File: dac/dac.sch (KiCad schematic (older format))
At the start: 0 parts

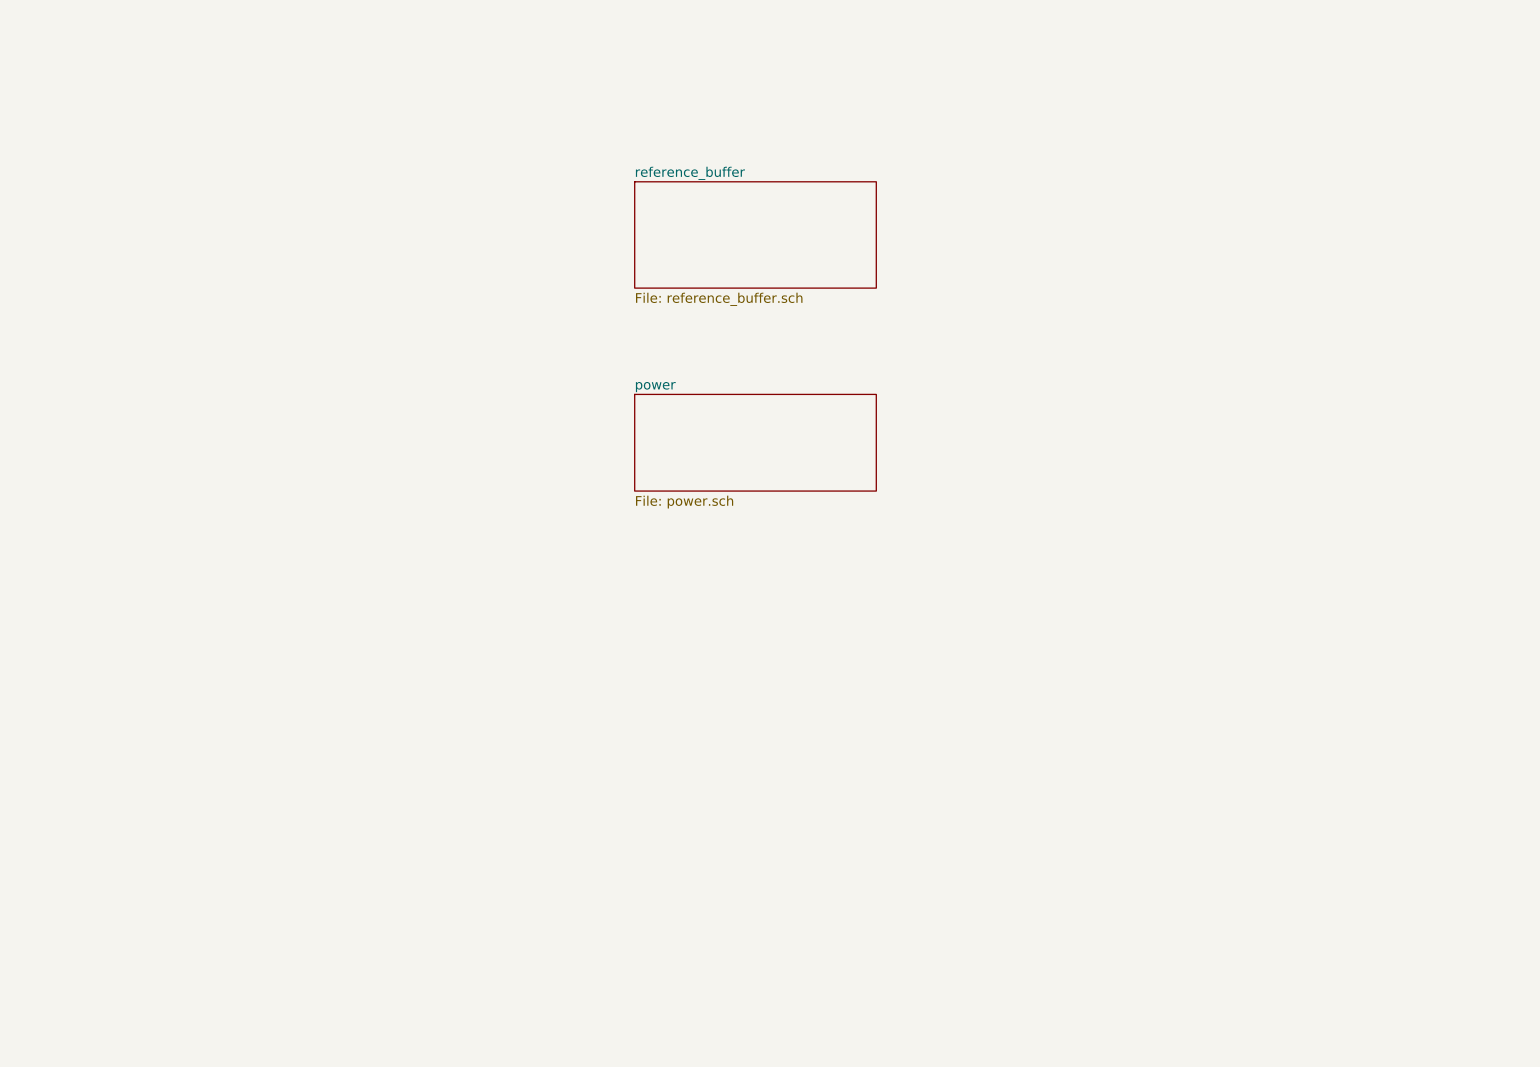
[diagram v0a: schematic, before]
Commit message: Much progress on the DAC card.  Schematic is complete, starting on placement.
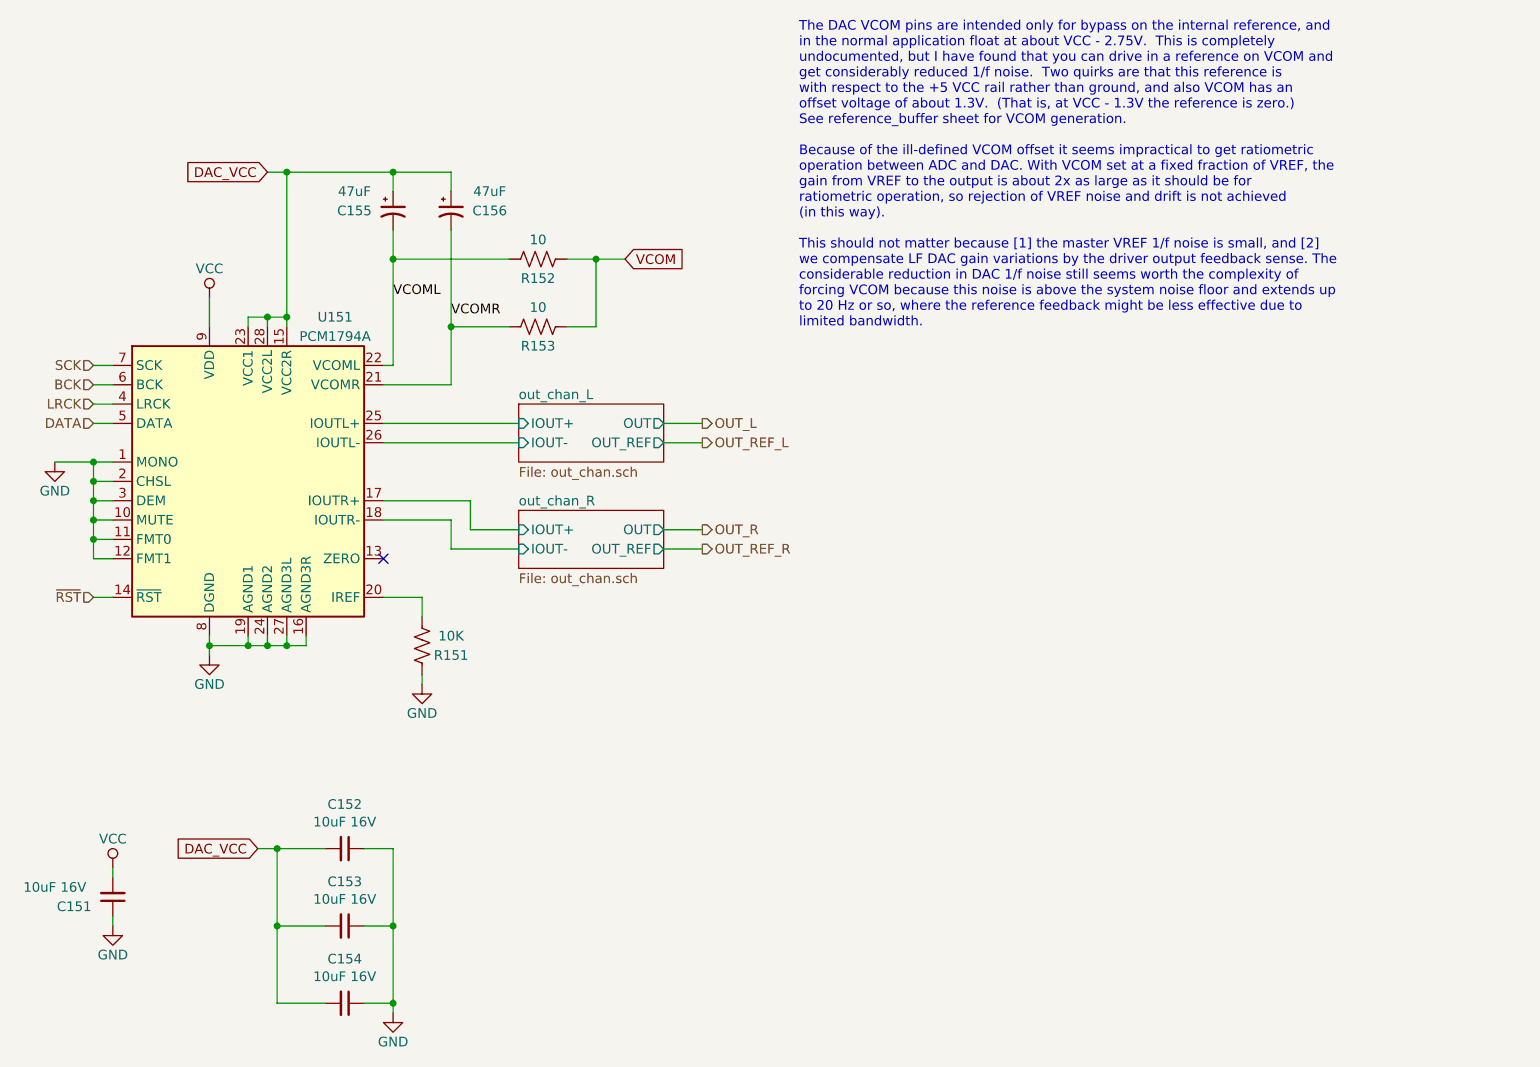
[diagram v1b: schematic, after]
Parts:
- added C151, C152, C153, C154: 10uF 16V, Capacitor_SMD:C_0805_2012Metric, symbol Device:C_Small
- added C155, C156: 47uF, Capacitor_SMD:CP_Elec_6.3x7.7, symbol Device:CP1_Small
- added R151: 10K, Resistor_SMD:R_0603_1608Metric, symbol Device:R_US
- added R152, R153: 10, Resistor_SMD:R_0805_2012Metric, symbol Device:R_US
- added U151: PCM1794A, Package_SO:SSOP-28_5.3x10.2mm_P0.65mm, symbol Audio:PCM1794A
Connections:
- new net: R151.2, U151.20 (IREF)
- new net BCK: U151.6 (BCK)
- new net DAC_VCC: C152.2, C153.2, C154.2, C155.1, C156.1, U151.15 (VCC2R), U151.23 (VCC1), U151.28 (VCC2L)
- new net DATA: U151.5 (DATA)
- new net GND: C151.1, C152.1, C153.1, C154.1, R151.1, U151.1 (MONO), U151.10 (MUTE), U151.11 (FMT0), U151.12 (FMT1), U151.16 (AGND3R), U151.19 (AGND1), U151.2 (CHSL), U151.24 (AGND2), U151.27 (AGND3L), U151.3 (DEM), U151.8 (DGND)
- new net LRCK: U151.4 (LRCK)
- new net SCK: U151.7 (SCK)
- new net VCC: C151.2, U151.9 (VDD)
- new net VCOM: R152.1, R153.1
- new net VCOML: C155.2, R152.2, U151.22 (VCOML)
- new net VCOMR: C156.2, R153.2, U151.21 (VCOMR)
- new net out_chan_L/IOUT+: U151.25 (IOUTL+)
- new net out_chan_L/IOUT-: U151.26 (IOUTL-)
- new net out_chan_R/IOUT+: U151.17 (IOUTR+)
- new net out_chan_R/IOUT-: U151.18 (IOUTR-)
- new net ~RST: U151.14 (~RST)
- no-connect marks 0 -> 1
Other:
- note added: "The DAC VCOM pins are intended only for bypass on the internal reference, and\nin the normal application float at about VCC - 2.75V. This is completely\nundocumented, but I have found that you can drive in a reference on VCOM and\nget considerably reduced 1/f noise. Two quirks are that this reference is\nwith respect to the +5 VCC rail rather than ground, and also VCOM has an\noffset voltage of a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"

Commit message: DAC board is routed.  I also changed the digital interface to use a buffer (like I did on the input board) so that everything is buffered and we don't have multi-drop nets.
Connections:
- net IREF: now reaches R151.2, U151.20 (IREF)
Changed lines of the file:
@@
 $Descr A4 11693 8268
 encoding utf-8
-Sheet 4 11
+Sheet 7 11
 Title ""
 Date ""
@@
 AR Path="/5F7EFEA4/5F7F1182" Ref="U151"  Part="1"
 AR Path="/5F8C3863/5F7F1182" Ref="U351"  Part="1"
-F 0 "U151" H 4250 5000 50  0000 C CNN
+F 0 "U351" H 4250 5000 50  0000 C CNN
 F 1 "PCM1794A" H 4250 4900 50  0000 C CNN
 F 2 "Package_SO:SSOP-28_5.3x10.2mm_P0.65mm" H 3800 4150 50  0001 C CNN
@@
 AR Path="/5F7EFEA4/5F839C4F" Ref="C154"  Part="1"
 AR Path="/5F8C3863/5F839C4F" Ref="C354"  Part="1"
-F 0 "C154" V 4071 6850 50  0000 C CNN
+F 0 "C354" V 4071 6850 50  0000 C CNN
 F 1 "10uF 16V" V 4162 6850 50  0000 C CNN
 F 2 "Capacitor_SMD:C_0805_2012Metric" H 4300 6850 50  0001 C CNN
@@
 AR Path="/5F7EFEA4/5F839CAC" Ref="C153"  Part="1"
 AR Path="/5F8C3863/5F839CAC" Ref="C353"  Part="1"
-F 0 "C153" V 4071 6450 50  0000 C CNN
+F 0 "C353" V 4071 6450 50  0000 C CNN
 F 1 "10uF 16V" V 4162 6450 50  0000 C CNN
 F 2 "Capacitor_SMD:C_0805_2012Metric" H 4300 6450 50  0001 C CNN
@@
 AR Path="/5F7EFEA4/5F83A16C" Ref="C152"  Part="1"
 AR Path="/5F8C3863/5F83A16C" Ref="C352"  Part="1"
-F 0 "C152" V 4071 6050 50  0000 C CNN
+F 0 "C352" V 4071 6050 50  0000 C CNN
 F 1 "10uF 16V" V 4162 6050 50  0000 C CNN
 F 2 "Capacitor_SMD:C_0805_2012Metric" H 4300 6050 50  0001 C CNN
@@
 AR Path="/5F7EFEA4/5F83FAF4" Ref="C151"  Part="1"
 AR Path="/5F8C3863/5F83FAF4" Ref="C351"  Part="1"
-F 0 "C151" H 3300 6350 50  0000 C CNN
+F 0 "C351" H 3300 6350 50  0000 C CNN
 F 1 "10uF 16V" H 3400 6250 50  0000 C CNN
 F 2 "Capacitor_SMD:C_0805_2012Metric" H 3100 6300 50  0001 C CNN
@@
 AR Path="/5F7EFEA4/5F854448" Ref="C155"  Part="1"
 AR Path="/5F8C3863/5F854448" Ref="C355"  Part="1"
-F 0 "C155" H 4350 2750 50  0000 C CNN
+F 0 "C355" H 4350 2750 50  0000 C CNN
 F 1 "47uF" H 4350 2850 50  0000 C CNN
 F 2 "Capacitor_SMD:CP_Elec_6.3x7.7" H 4550 2750 50  0001 C CNN
@@
 AR Path="/5F7EFEA4/5F8572D4" Ref="C156"  Part="1"
 AR Path="/5F8C3863/5F8572D4" Ref="C356"  Part="1"
-F 0 "C156" H 5050 2750 50  0000 C CNN
+F 0 "C356" H 5050 2750 50  0000 C CNN
 F 1 "47uF" H 5050 2850 50  0000 C CNN
 F 2 "Capacitor_SMD:CP_Elec_6.3x7.7" H 4850 2750 50  0001 C CNN
@@
 AR Path="/5F7EFEA4/5F8612BE" Ref="R153"  Part="1"
 AR Path="/5F8C3863/5F8612BE" Ref="R353"  Part="1"
-F 0 "R153" V 5400 3350 50  0000 C CNN
+F 0 "R353" V 5400 3350 50  0000 C CNN
 F 1 "10" V 5200 3350 50  0000 C CNN
 F 2 "Resistor_SMD:R_0805_2012Metric" V 5340 3340 50  0001 C CNN
@@
 AR Path="/5F7EFEA4/5F861966" Ref="R152"  Part="1"
 AR Path="/5F8C3863/5F861966" Ref="R352"  Part="1"
-F 0 "R152" V 5400 3000 50  0000 C CNN
+F 0 "R352" V 5400 3000 50  0000 C CNN
 F 1 "10" V 5200 3000 50  0000 C CNN
 F 2 "Resistor_SMD:R_0805_2012Metric" V 5340 2990 50  0001 C CNN
@@
 AR Path="/5F7EFEA4/5F86B07A" Ref="R151"  Part="1"
 AR Path="/5F8C3863/5F86B07A" Ref="R351"  Part="1"
-F 0 "R151" H 4550 5050 50  0000 C CNN
+F 0 "R351" H 4550 5050 50  0000 C CNN
 F 1 "10K" H 4550 4950 50  0000 C CNN
 F 2 "Resistor_SMD:R_0603_1608Metric" V 4740 4990 50  0001 C CNN
@@
 Connection ~ 4550 3000
 $Sheet
+S 5200 4300 750  300
+U 5F8AE34F
+F0 "out_chan_R" 50
+F1 "out_chan.sch" 50
+F2 "IOUT+" I L 5200 4400 50
+F3 "IOUT-" I L 5200 4500 50
+F4 "OUT" O R 5950 4400 50
+F5 "OUT_REF" O R 5950 4500 50
+$EndSheet
+Wire Wire Line
+	5200 3850 4500 3850
+Wire Wire Line
+	5200 3950 4500 3950
+$Sheet
 S 5200 3750 750  300
-U 5F8AE34F
+U 5F8B0DF1
 F0 "out_chan_L" 50
 F1 "out_chan.sch" 50
@@
 F4 "OUT" O R 5950 3850 50
 F5 "OUT_REF" O R 5950 3950 50
-$EndSheet
-Wire Wire Line
-	5200 3850 4500 3850
-Wire Wire Line
-	5200 3950 4500 3950
-$Sheet
-S 5200 4300 750  300
-U 5F8B0DF1
-F0 "out_chan_R" 50
-F1 "out_chan.sch" 50
-F2 "IOUT+" I L 5200 4400 50
-F3 "IOUT-" I L 5200 4500 50
-F4 "OUT" O R 5950 4400 50
-F5 "OUT_REF" O R 5950 4500 50
 $EndSheet
 Wire Wire Line
@@
 Text Label 4850 3300 0    50   ~ 0
 VCOMR
+Text Label 4550 4750 0    50   ~ 0
+IREF
 $EndSCHEMATC

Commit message: Everything seems ready to go for the DAC board.  Made my BOM and checked it twice. Checked footprints of new components and fixed J5, R7-R10.
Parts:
- C151, C152, C153, C154: DK line 10 -> M.10
- C155, C156: DK line (none) -> D.5
- R151: DK line (none) -> I.56; Description (none) -> RES SMD 10K OHM 0.1% 1/10W 0603; Digikey (none) -> P10KDBCT-ND; MPN (none) -> ERA-3AEB103V; Manufacturer (none) -> Panasonic Electronic Components
- R152, R153: DK line 52 -> I.52
- U151: DK line (none) -> D.4; Description (none) -> IC DAC/AUDIO 24BIT 200K 28SSOP; Digikey (none) -> 296-21537-1-ND; MPN (none) -> PCM1794ADBR; Manufacturer (none) -> Texas Instruments
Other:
- note added: "One DAC chip with two output channels\nTwo instances of this sheet in all"
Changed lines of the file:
@@
 $Descr A4 11693 8268
 encoding utf-8
-Sheet 7 11
+Sheet 4 11
 Title ""
 Date ""
@@
 AR Path="/5F7EFEA4/5F7F1182" Ref="U151"  Part="1"
 AR Path="/5F8C3863/5F7F1182" Ref="U351"  Part="1"
-F 0 "U351" H 4250 5000 50  0000 C CNN
+F 0 "U151" H 4250 5000 50  0000 C CNN
 F 1 "PCM1794A" H 4250 4900 50  0000 C CNN
 F 2 "Package_SO:SSOP-28_5.3x10.2mm_P0.65mm" H 3800 4150 50  0001 C CNN
 F 3 "http://www.ti.com/lit/ds/symlink/pcm1794a.pdf" H 3800 4150 50  0001 C CNN
+F 4 "D.4" H 3800 4150 50  0001 C CNN "DK line"
+F 5 "IC DAC/AUDIO 24BIT 200K 28SSOP" H 3800 4150 50  0001 C CNN "Description"
+F 6 "296-21537-1-ND" H 3800 4150 50  0001 C CNN "Digikey"
+F 7 "PCM1794ADBR" H 3800 4150 50  0001 C CNN "MPN"
+F 8 "Texas Instruments" H 3800 4150 50  0001 C CNN "Manufacturer"
 	1    3800 4150
 	1    0    0    -1
@@
 AR Path="/5F7EFEA4/5F839C4F" Ref="C154"  Part="1"
 AR Path="/5F8C3863/5F839C4F" Ref="C354"  Part="1"
-F 0 "C354" V 4071 6850 50  0000 C CNN
+F 0 "C154" V 4071 6850 50  0000 C CNN
 F 1 "10uF 16V" V 4162 6850 50  0000 C CNN
 F 2 "Capacitor_SMD:C_0805_2012Metric" H 4300 6850 50  0001 C CNN
@@
 F 5 "399-8012-1-ND" H 4300 6850 50  0001 C CNN "Digikey"
 F 6 "C0805C106K4PACTU" H 4300 6850 50  0001 C CNN "MPN"
-F 7 "10" H 4300 6850 50  0001 C CNN "DK line"
+F 7 "M.10" H 4300 6850 50  0001 C CNN "DK line"
 F 8 "" H 4300 6850 50  0001 C CNN "MFG"
 F 9 "KEMET" H 4300 6850 50  0001 C CNN "Manufacturer"
@@
 AR Path="/5F7EFEA4/5F839CAC" Ref="C153"  Part="1"
 AR Path="/5F8C3863/5F839CAC" Ref="C353"  Part="1"
-F 0 "C353" V 4071 6450 50  0000 C CNN
+F 0 "C153" V 4071 6450 50  0000 C CNN
 F 1 "10uF 16V" V 4162 6450 50  0000 C CNN
 F 2 "Capacitor_SMD:C_0805_2012Metric" H 4300 6450 50  0001 C CNN
@@
 F 5 "399-8012-1-ND" H 4300 6450 50  0001 C CNN "Digikey"
 F 6 "C0805C106K4PACTU" H 4300 6450 50  0001 C CNN "MPN"
-F 7 "10" H 4300 6450 50  0001 C CNN "DK line"
+F 7 "M.10" H 4300 6450 50  0001 C CNN "DK line"
 F 8 "" H 4300 6450 50  0001 C CNN "MFG"
 F 9 "KEMET" H 4300 6450 50  0001 C CNN "Manufacturer"
@@
 AR Path="/5F7EFEA4/5F83A16C" Ref="C152"  Part="1"
 AR Path="/5F8C3863/5F83A16C" Ref="C352"  Part="1"
-F 0 "C352" V 4071 6050 50  0000 C CNN
+F 0 "C152" V 4071 6050 50  0000 C CNN
 F 1 "10uF 16V" V 4162 6050 50  0000 C CNN
 F 2 "Capacitor_SMD:C_0805_2012Metric" H 4300 6050 50  0001 C CNN
@@
 F 5 "399-8012-1-ND" H 4300 6050 50  0001 C CNN "Digikey"
 F 6 "C0805C106K4PACTU" H 4300 6050 50  0001 C CNN "MPN"
-F 7 "10" H 4300 6050 50  0001 C CNN "DK line"
+F 7 "M.10" H 4300 6050 50  0001 C CNN "DK line"
 F 8 "" H 4300 6050 50  0001 C CNN "MFG"
 F 9 "KEMET" H 4300 6050 50  0001 C CNN "Manufacturer"
@@
 AR Path="/5F7EFEA4/5F83FAF4" Ref="C151"  Part="1"
 AR Path="/5F8C3863/5F83FAF4" Ref="C351"  Part="1"
-F 0 "C351" H 3300 6350 50  0000 C CNN
+F 0 "C151" H 3300 6350 50  0000 C CNN
 F 1 "10uF 16V" H 3400 6250 50  0000 C CNN
 F 2 "Capacitor_SMD:C_0805_2012Metric" H 3100 6300 50  0001 C CNN
@@
 F 5 "399-8012-1-ND" H 3100 6300 50  0001 C CNN "Digikey"
 F 6 "C0805C106K4PACTU" H 3100 6300 50  0001 C CNN "MPN"
-F 7 "10" H 3100 6300 50  0001 C CNN "DK line"
+F 7 "M.10" H 3100 6300 50  0001 C CNN "DK line"
 F 8 "" H 3100 6300 50  0001 C CNN "MFG"
 F 9 "KEMET" H 3100 6300 50  0001 C CNN "Manufacturer"
@@
 AR Path="/5F7EFEA4/5F854448" Ref="C155"  Part="1"
 AR Path="/5F8C3863/5F854448" Ref="C355"  Part="1"
-F 0 "C355" H 4350 2750 50  0000 C CNN
+F 0 "C155" H 4350 2750 50  0000 C CNN
 F 1 "47uF" H 4350 2850 50  0000 C CNN
 F 2 "Capacitor_SMD:CP_Elec_6.3x7.7" H 4550 2750 50  0001 C CNN
-F 3 "?" H 4550 2750 50  0001 C CNN
+F 3 "http://www.chemi-con.co.jp/cgi-bin/CAT_DB/SEARCH/cat_db_al.cgi?e=e&j=p&pdfname=hxd" H 4550 2750 50  0001 C CNN
 F 4 "CAP ALUM HYBRID 47UF 20% 35V SMD" H 4550 2750 50  0001 C CNN "Description"
 F 5 "565-HHXD350ARA470MF80GCT-ND" H 4550 2750 50  0001 C CNN "Digikey"
 F 6 "HHXD350ARA470MF80G" H 4550 2750 50  0001 C CNN "MPN"
-F 7 "" H 4550 2750 50  0001 C CNN "DK line"
+F 7 "D.5" H 4550 2750 50  0001 C CNN "DK line"
 F 8 "United Chemi-Con" H 4550 2750 50  0001 C CNN "Manufacturer"
 	1    4550 2750
@@
 AR Path="/5F7EFEA4/5F8572D4" Ref="C156"  Part="1"
 AR Path="/5F8C3863/5F8572D4" Ref="C356"  Part="1"
-F 0 "C356" H 5050 2750 50  0000 C CNN
+F 0 "C156" H 5050 2750 50  0000 C CNN
 F 1 "47uF" H 5050 2850 50  0000 C CNN
 F 2 "Capacitor_SMD:CP_Elec_6.3x7.7" H 4850 2750 50  0001 C CNN
-F 3 "?" H 4850 2750 50  0001 C CNN
+F 3 "http://www.chemi-con.co.jp/cgi-bin/CAT_DB/SEARCH/cat_db_al.cgi?e=e&j=p&pdfname=hxd" H 4850 2750 50  0001 C CNN
 F 4 "CAP ALUM HYBRID 47UF 20% 35V SMD" H 4850 2750 50  0001 C CNN "Description"
 F 5 "565-HHXD350ARA470MF80GCT-ND" H 4850 2750 50  0001 C CNN "Digikey"
 F 6 "HHXD350ARA470MF80G" H 4850 2750 50  0001 C CNN "MPN"
-F 7 "" H 4850 2750 50  0001 C CNN "DK line"
+F 7 "D.5" H 4850 2750 50  0001 C CNN "DK line"
 F 8 "United Chemi-Con" H 4850 2750 50  0001 C CNN "Manufacturer"
 	1    4850 2750
@@
 AR Path="/5F7EFEA4/5F8612BE" Ref="R153"  Part="1"
 AR Path="/5F8C3863/5F8612BE" Ref="R353"  Part="1"
-F 0 "R353" V 5400 3350 50  0000 C CNN
+F 0 "R153" V 5400 3350 50  0000 C CNN
 F 1 "10" V 5200 3350 50  0000 C CNN
 F 2 "Resistor_SMD:R_0805_2012Metric" V 5340 3340 50  0001 C CNN
 F 3 "http://www.vishay.com/docs/20043/crcwhpe3.pdf" H 5300 3350 50  0001 C CNN
 F 4 "541-10TACT-ND" H 5300 3350 50  0001 C CNN "Digikey"
-F 5 "52" H 5300 3350 50  0001 C CNN "DK line"
+F 5 "I.52" H 5300 3350 50  0001 C CNN "DK line"
 F 6 "RES SMD 10 OHM 5% 1/2W 0805" H 5300 3350 50  0001 C CNN "Description"
 F 7 "CRCW080510R0JNEAHP" H 5300 3350 50  0001 C CNN "MPN"
@@
 AR Path="/5F7EFEA4/5F861966" Ref="R152"  Part="1"
 AR Path="/5F8C3863/5F861966" Ref="R352"  Part="1"
-F 0 "R352" V 5400 3000 50  0000 C CNN
+F 0 "R152" V 5400 3000 50  0000 C CNN
 F 1 "10" V 5200 3000 50  0000 C CNN
 F 2 "Resistor_SMD:R_0805_2012Metric" V 5340 2990 50  0001 C CNN
 F 3 "http://www.vishay.com/docs/20043/crcwhpe3.pdf" H 5300 3000 50  0001 C CNN
 F 4 "541-10TACT-ND" H 5300 3000 50  0001 C CNN "Digikey"
-F 5 "52" H 5300 3000 50  0001 C CNN "DK line"
+F 5 "I.52" H 5300 3000 50  0001 C CNN "DK line"
 F 6 "RES SMD 10 OHM 5% 1/2W 0805" H 5300 3000 50  0001 C CNN "Description"
 F 7 "CRCW080510R0JNEAHP" H 5300 3000 50  0001 C CNN "MPN"
@@
 AR Path="/5F7EFEA4/5F86B07A" Ref="R151"  Part="1"
 AR Path="/5F8C3863/5F86B07A" Ref="R351"  Part="1"
-F 0 "R351" H 4550 5050 50  0000 C CNN
+F 0 "R151" H 4550 5050 50  0000 C CNN
 F 1 "10K" H 4550 4950 50  0000 C CNN
 F 2 "Resistor_SMD:R_0603_1608Metric" V 4740 4990 50  0001 C CNN
-F 3 "~" H 4700 5000 50  0001 C CNN
+F 3 "https://industrial.panasonic.com/cdbs/www-data/pdf/RDM0000/AOA0000C307.pdf" H 4700 5000 50  0001 C CNN
+F 4 "I.56" H 4700 5000 50  0001 C CNN "DK line"
+F 5 "RES SMD 10K OHM 0.1% 1/10W 0603" H 4700 5000 50  0001 C CNN "Description"
+F 6 "P10KDBCT-ND" H 4700 5000 50  0001 C CNN "Digikey"
+F 7 "ERA-3AEB103V" H 4700 5000 50  0001 C CNN "MPN"
+F 8 "Panasonic Electronic Components" H 4700 5000 50  0001 C CNN "Manufacturer"
 	1    4700 5000
 	-1   0    0    1
@@
 AR Path="/5F7EFEA4/5F9ED561" Ref="#PWR0113"  Part="1"
 AR Path="/5F8C3863/5F9ED561" Ref="#PWR0117"  Part="1"
-F 0 "#PWR0117" H 3600 3050 50  0001 C CNN
+F 0 "#PWR0113" H 3600 3050 50  0001 C CNN
 F 1 "VCC" H 3600 3350 50  0000 C CNN
 F 2 "" H 3600 3200 50  0001 C CNN
@@
 AR Path="/5F7EFEA4/5F9F1229" Ref="#PWR0116"  Part="1"
 AR Path="/5F8C3863/5F9F1229" Ref="#PWR0125"  Part="1"
-F 0 "#PWR0125" H 3100 6000 50  0001 C CNN
+F 0 "#PWR0116" H 3100 6000 50  0001 C CNN
 F 1 "VCC" H 3100 6300 50  0000 C CNN
 F 2 "" H 3100 6150 50  0001 C CNN
@@
 AR Path="/5F7EFEA4/5F8A8A2A" Ref="#PWR0146"  Part="1"
 AR Path="/5F8C3863/5F8A8A2A" Ref="#PWR0151"  Part="1"
-F 0 "#PWR0151" H 4700 4950 50  0001 C CNN
+F 0 "#PWR0146" H 4700 4950 50  0001 C CNN
 F 1 "GND" H 4700 5050 50  0000 C CNN
 F 2 "" H 4700 5200 50  0001 C CNN
@@
 AR Path="/5F7EFEA4/5F8AA834" Ref="#PWR0147"  Part="1"
 AR Path="/5F8C3863/5F8AA834" Ref="#PWR0152"  Part="1"
-F 0 "#PWR0152" H 3600 4800 50  0001 C CNN
+F 0 "#PWR0147" H 3600 4800 50  0001 C CNN
 F 1 "GND" H 3600 4900 50  0000 C CNN
 F 2 "" H 3600 5050 50  0001 C CNN
@@
 AR Path="/5F7EFEA4/5F8AABB7" Ref="#PWR0148"  Part="1"
 AR Path="/5F8C3863/5F8AABB7" Ref="#PWR0153"  Part="1"
-F 0 "#PWR0153" H 2800 3800 50  0001 C CNN
+F 0 "#PWR0148" H 2800 3800 50  0001 C CNN
 F 1 "GND" H 2800 3900 50  0000 C CNN
 F 2 "" H 2800 4050 50  0001 C CNN
@@
 AR Path="/5F7EFEA4/5F8AB0BD" Ref="#PWR0149"  Part="1"
 AR Path="/5F8C3863/5F8AB0BD" Ref="#PWR0154"  Part="1"
-F 0 "#PWR0154" H 4550 6650 50  0001 C CNN
+F 0 "#PWR0149" H 4550 6650 50  0001 C CNN
 F 1 "GND" H 4550 6750 50  0000 C CNN
 F 2 "" H 4550 6900 50  0001 C CNN
@@
 AR Path="/5F7EFEA4/5F8AB4CB" Ref="#PWR0150"  Part="1"
 AR Path="/5F8C3863/5F8AB4CB" Ref="#PWR0155"  Part="1"
-F 0 "#PWR0155" H 3100 6200 50  0001 C CNN
+F 0 "#PWR0150" H 3100 6200 50  0001 C CNN
 F 1 "GND" H 3100 6300 50  0000 C CNN
 F 2 "" H 3100 6450 50  0001 C CNN
@@
 Text Label 4550 4750 0    50   ~ 0
 IREF
+Text Notes 7100 6900 0    50   ~ 0
+One DAC chip with two output channels\nTwo instances of this sheet in all
 $EndSCHEMATC
